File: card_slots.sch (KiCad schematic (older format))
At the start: 0 parts

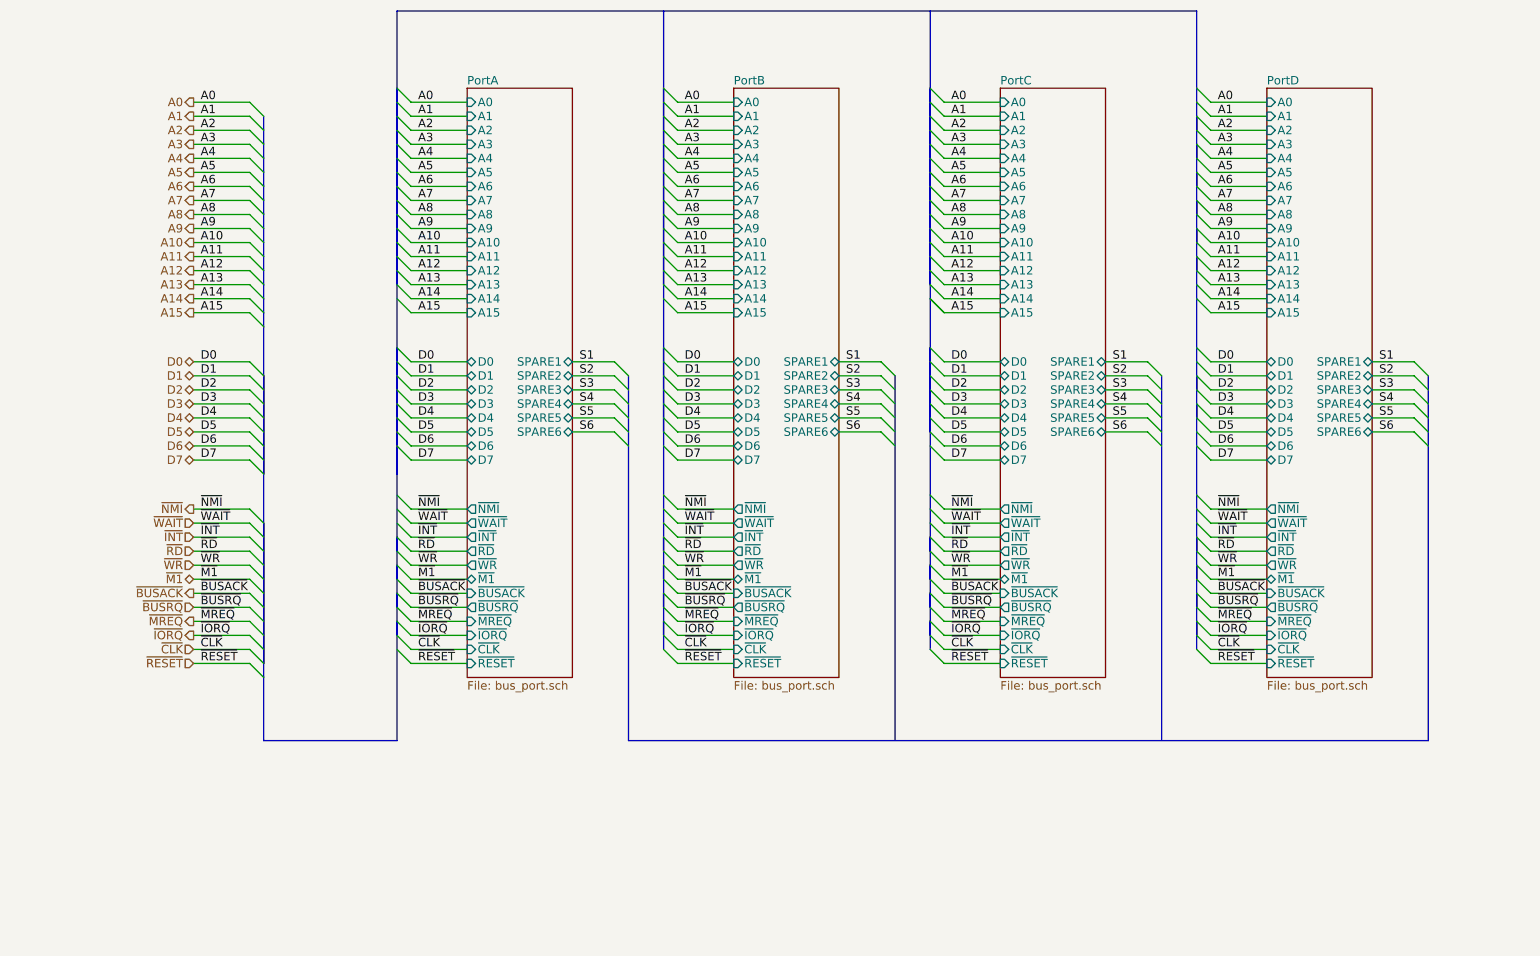
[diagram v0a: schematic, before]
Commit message: Update with smaller board and through-hole parts.
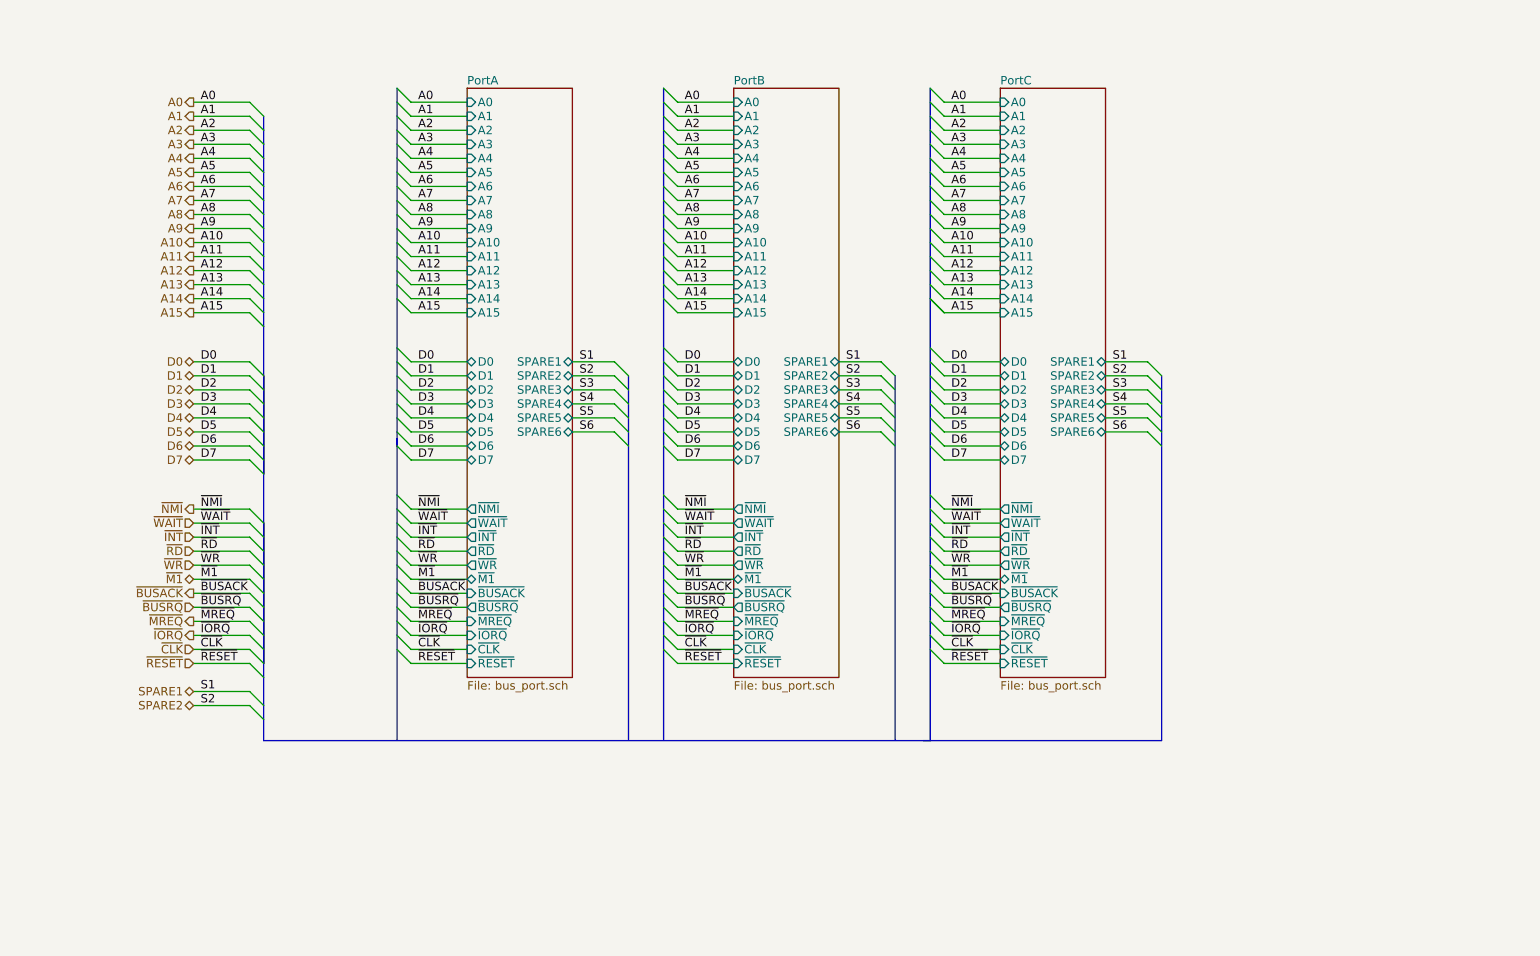
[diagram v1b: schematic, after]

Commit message: New layout complete. Now with rc2014 compat. slots!
Plus on board address decoding, single stepping using M1 line so button
is click per instruction. Board is also much smaller!
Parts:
- added C7: 100n, Capacitors_ThroughHole:C_Rect_L4_W2.5_P2.5, symbol C
- added U3: 74LS138, Housings_DIP:DIP-16_W7.62mm_LongPads, symbol 74LS138
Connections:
- net labels added: GND, RX, TX, VCC, ~IOSEL1, ~IOSEL2, ~IOSEL3, ~IOSEL4, ~IOSEL5, ~IOSEL6, ~IOSEL7, ~IOSEL8
- net labels removed: S5, S6, SPARE1, SPARE2
- wire segments 164 -> 303

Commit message: * Replaced one card slot with an updated expansion connector. * Replaced '138 with GAL. * Implemented interrupt priority lines IEI/IEO. * Replaced discrete oscillator with 14/8 pin DIP oscillator block.
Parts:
- removed U3: 74LS138, Housings_DIP:DIP-16_W7.62mm_LongPads, symbol 74LS138
- added P3: Jumper, symbol CONN_01X03
- added U3: ATF16V8CV, symbol ATF16V8CV
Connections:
- net labels added: IEI, IEO, SPARE1, SPARE2, SPARE3, SPARE4, ~IOREQ, ~IOSEL0
- net labels removed: ~IOSEL4, ~IOSEL5, ~IOSEL6, ~IOSEL7, ~IOSEL8
- wire segments 303 -> 276

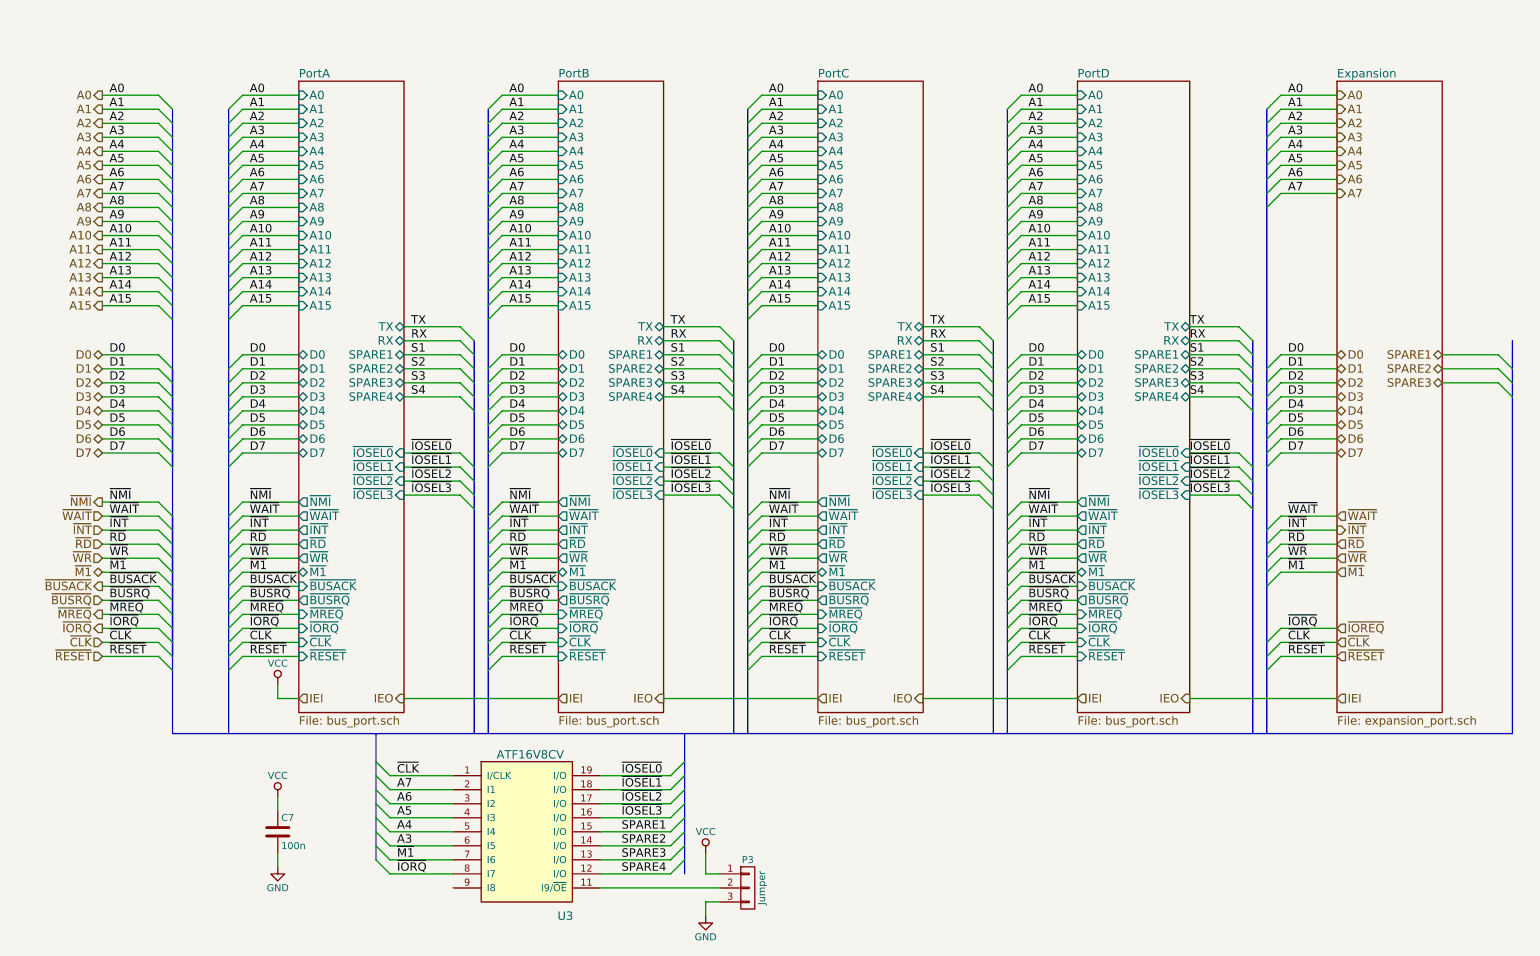
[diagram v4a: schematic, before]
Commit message: Fixed schema DRC errors
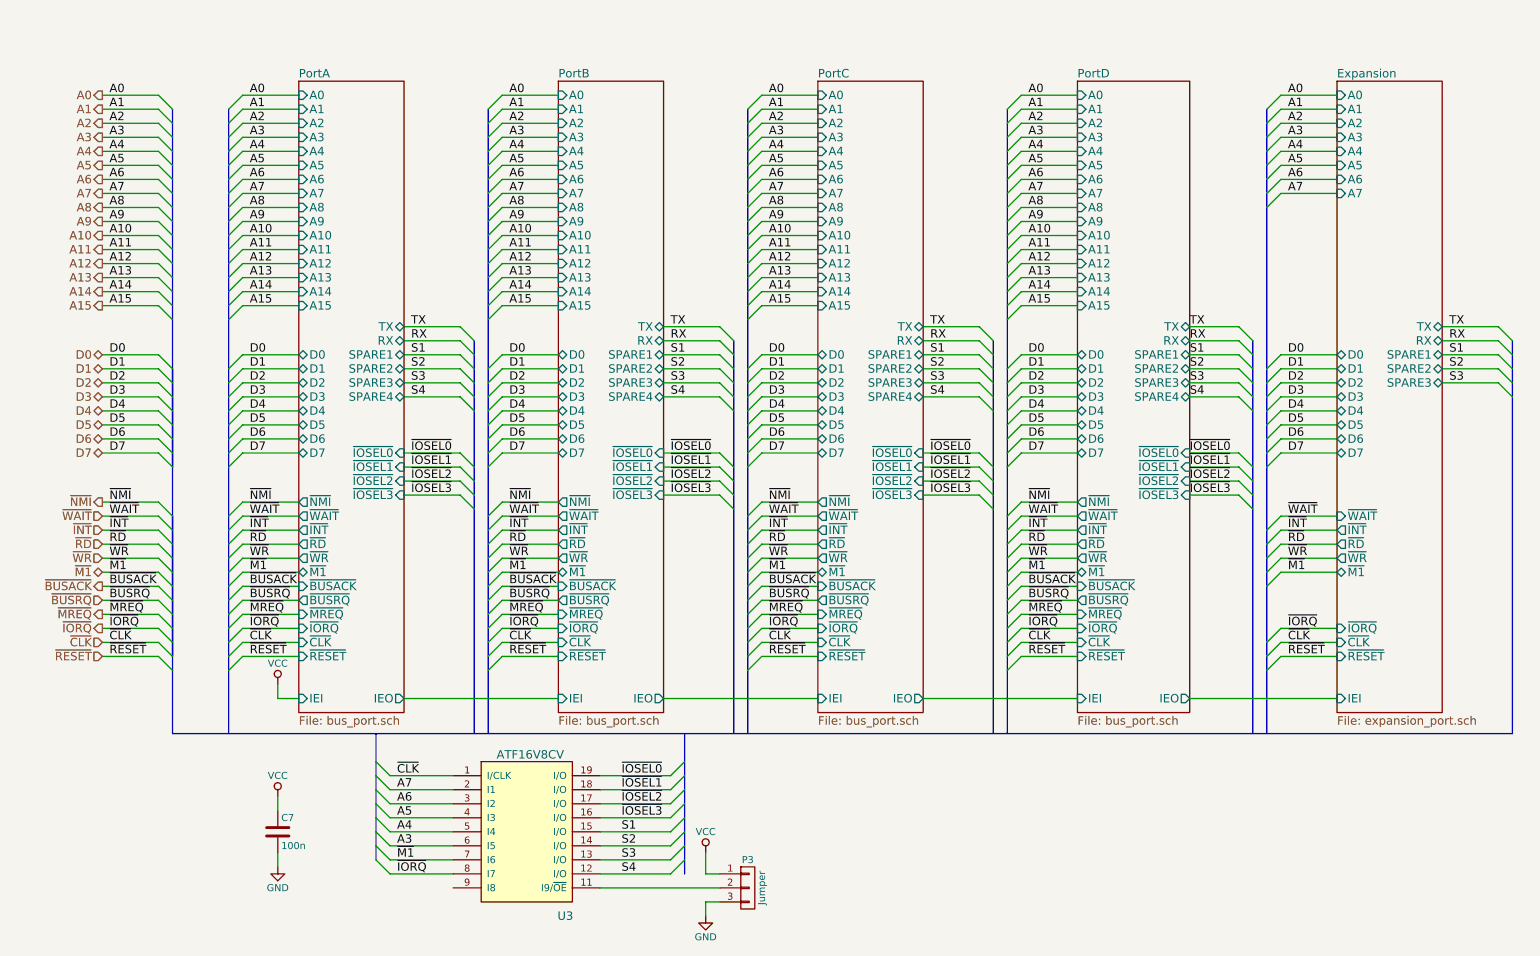
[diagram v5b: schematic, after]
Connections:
- net SPARE1 is gone; now on net S1: U3.15 (I/O)
- net SPARE2 is gone; now on net S2: U3.14 (I/O)
- net SPARE3 is gone; now on net S3: U3.13 (I/O)
- net SPARE4 is gone; now on net S4: U3.12 (I/O)
- net ~IOREQ renamed ~IORQ
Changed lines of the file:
@@
 F46 "~IOSEL2" I R 3200 4450 60
 F47 "~IOSEL3" I R 3200 4550 60
+F48 "IEI" I L 2450 6000 60
+F49 "IEO" O R 3200 6000 60
 $EndSheet
 Entry Wire Line
@@
 F46 "~IOSEL2" I R 5050 4450 60
 F47 "~IOSEL3" I R 5050 4550 60
+F48 "IEI" I L 4300 6000 60
+F49 "IEO" O R 5050 6000 60
 $EndSheet
 Entry Wire Line
@@
 F46 "~IOSEL2" I R 6900 4450 60
 F47 "~IOSEL3" I R 6900 4550 60
+F48 "IEI" I L 6150 6000 60
+F49 "IEO" O R 6900 6000 60
 $EndSheet
 Entry Wire Line
@@
 F46 "~IOSEL2" I R 8800 4450 60
 F47 "~IOSEL3" I R 8800 4550 60
+F48 "IEI" I L 8000 6000 60
+F49 "IEO" O R 8800 6000 60
 $EndSheet
 Entry Wire Line
@@
 $EndComp
 $Comp
-L VCC #PWR25
+L VCC #PWR020
 U 1 1 5797F3F2
 P 2300 6700
-F 0 "#PWR25" H 2300 6550 50  0001 C CNN
+F 0 "#PWR020" H 2300 6550 50  0001 C CNN
 F 1 "VCC" H 2300 6850 50  0000 C CNN
 F 2 "" H 2300 6700 50  0000 C CNN
@@
 $EndComp
 $Comp
-L GND #PWR26
+L GND #PWR021
 U 1 1 5797F8BA
 P 2300 7200
-F 0 "#PWR26" H 2300 6950 50  0001 C CNN
+F 0 "#PWR021" H 2300 6950 50  0001 C CNN
 F 1 "GND" H 2300 7050 50  0000 C CNN
 F 2 "" H 2300 7200 50  0000 C CNN
@@
 	1    0    0    -1
 $EndComp
-Text HLabel 2450 6000 2    60   Input ~ 0
-IEI
-Text HLabel 4300 6000 2    60   Input ~ 0
-IEI
-Text HLabel 6150 6000 2    60   Input ~ 0
-IEI
-Text HLabel 8000 6000 2    60   Input ~ 0
-IEI
-Text HLabel 3200 6000 0    60   Output ~ 0
-IEO
-Text HLabel 5050 6000 0    60   Output ~ 0
-IEO
-Text HLabel 6900 6000 0    60   Output ~ 0
-IEO
-Text HLabel 8800 6000 0    60   Output ~ 0
-IEO
 $Comp
-L VCC #PWR24
+L VCC #PWR022
 U 1 1 57AEADAF
 P 2300 5900
-F 0 "#PWR24" H 2300 5750 50  0001 C CNN
+F 0 "#PWR022" H 2300 5750 50  0001 C CNN
 F 1 "VCC" H 2300 6050 50  0000 C CNN
 F 2 "" H 2300 5900 50  0000 C CNN
@@
 	5100 7250 5200 7150
 Text Label 4750 6950 0    60   ~ 0
-SPARE1
+S1
 Text Label 4750 7050 0    60   ~ 0
-SPARE2
+S2
 Text Label 4750 7150 0    60   ~ 0
-SPARE3
+S3
 Text Label 4750 7250 0    60   ~ 0
-SPARE4
+S4
 $Comp
-L GND #PWR28
+L GND #PWR023
 U 1 1 57B78722
 P 5350 7550
-F 0 "#PWR28" H 5350 7300 50  0001 C CNN
+F 0 "#PWR023" H 5350 7300 50  0001 C CNN
 F 1 "GND" H 5350 7400 50  0000 C CNN
 F 2 "" H 5350 7550 50  0000 C CNN
@@
 $EndComp
 $Comp
-L VCC #PWR27
+L VCC #PWR024
 U 1 1 57B83991
 P 5350 7100
-F 0 "#PWR27" H 5350 6950 50  0001 C CNN
+F 0 "#PWR024" H 5350 6950 50  0001 C CNN
 F 1 "VCC" H 5350 7250 50  0000 C CNN
 F 2 "" H 5350 7100 50  0000 C CNN
@@
 	1    0    0    -1
 $EndComp
-$Sheet
-S 9850 1600 750  4500
-U 57BB639D
-F0 "Expansion" 60
-F1 "expansion_port.sch" 60
-$EndSheet
-Text HLabel 9850 1700 2    60   Output ~ 0
-A0
-Text HLabel 9850 1800 2    60   Output ~ 0
-A1
-Text HLabel 9850 1900 2    60   Output ~ 0
-A2
-Text HLabel 9850 2000 2    60   Output ~ 0
-A3
-Text HLabel 9850 2100 2    60   Output ~ 0
-A4
-Text HLabel 9850 2200 2    60   Output ~ 0
-A5
-Text HLabel 9850 2300 2    60   Output ~ 0
-A6
-Text HLabel 9850 2400 2    60   Output ~ 0
-A7
-Text HLabel 9850 3550 2    60   BiDi ~ 0
-D0
-Text HLabel 9850 3650 2    60   BiDi ~ 0
-D1
-Text HLabel 9850 3750 2    60   BiDi ~ 0
-D2
-Text HLabel 9850 3850 2    60   BiDi ~ 0
-D3
-Text HLabel 9850 3950 2    60   BiDi ~ 0
-D4
-Text HLabel 9850 4050 2    60   BiDi ~ 0
-D5
-Text HLabel 9850 4150 2    60   BiDi ~ 0
-D6
-Text HLabel 9850 4250 2    60   BiDi ~ 0
-D7
-Text HLabel 9850 4700 2    60   Input ~ 0
-~WAIT
-Text HLabel 9850 4800 2    60   Output ~ 0
-~INT
-Text HLabel 9850 4900 2    60   Input ~ 0
-~RD
-Text HLabel 9850 5000 2    60   Input ~ 0
-~WR
-Text HLabel 9850 5100 2    60   Input ~ 0
-~M1
-Text HLabel 9850 5500 2    60   Input ~ 0
-~IOREQ
-Text HLabel 9850 5600 2    60   Input ~ 0
-~CLK
-Text HLabel 9850 5700 2    60   Input ~ 0
-~RESET
 Entry Wire Line
 	11000 3550 11100 3650
@@
 Wire Wire Line
 	10600 3650 11000 3650
-Text HLabel 10600 3650 0    60   BiDi ~ 0
-SPARE2
-Text HLabel 10600 3750 0    60   BiDi ~ 0
-SPARE3
-Text HLabel 10600 3550 0    60   BiDi ~ 0
-SPARE1
 Wire Wire Line
 	10600 3550 11000 3550
-Text HLabel 9850 6000 2    60   Input ~ 0
-IEI
 Wire Wire Line
 	8800 6000 9850 6000
+$Sheet
+S 9850 1600 750  4500
+U 57BB639D
+F0 "Expansion" 60
+F1 "expansion_port.sch" 60
+F2 "A0" I L 9850 1700 60
+F3 "A1" I L 9850 1800 60
+F4 "A2" I L 9850 1900 60
+F5 "A3" I L 9850 2000 60
+F6 "A4" I L 9850 2100 60
+F7 "A5" I L 9850 2200 60
+F8 "A6" I L 9850 2300 60
+F9 "A7" I L 9850 2400 60
+F10 "D0" T L 9850 3550 60
+F11 "D1" T L 9850 3650 60
+F12 "D2" T L 9850 3750 60
+F13 "D3" T L 9850 3850 60
+F14 "D4" T L 9850 3950 60
+F15 "D5" T L 9850 4050 60
+F16 "D6" T L 9850 4150 60
+F17 "D7" T L 9850 4250 60
+F18 "~M1" T L 9850 5100 60
+F19 "~IORQ" I L 9850 5500 60
+F20 "SPARE1" B R 10600 3550 60
+F21 "SPARE2" B R 10600 3650 60
+F22 "SPARE3" B R 10600 3750 60
+F23 "~RESET" I L 9850 5700 60
+F24 "~CLK" I L 9850 5600 60
+F25 "~INT" O L 9850 4800 60
+F26 "~WR" O L 9850 5000 60
+F27 "~RD" O L 9850 4900 60
+F28 "IEI" I L 9850 6000 60
+F29 "RX" B R 10600 3450 60
+F30 "TX" B R 10600 3350 60
+F31 "~WAIT" I L 9850 4700 60
+$EndSheet
+Entry Wire Line
+	11000 3350 11100 3450
+Entry Wire Line
+	11000 3450 11100 3550
+Wire Wire Line
+	10600 3350 11000 3350
+Wire Wire Line
+	10600 3450 11000 3450
+Text Label 10650 3550 0    60   ~ 0
+S1
+Text Label 10650 3650 0    60   ~ 0
+S2
+Text Label 10650 3750 0    60   ~ 0
+S3
+Text Label 10650 3350 0    60   ~ 0
+TX
+Text Label 10650 3450 0    60   ~ 0
+RX
 $EndSCHEMATC

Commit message: Added new expansion and GAL to layout.
Haven't routed the osc. or the reset.
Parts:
- P3: footprint (none) -> Pin_Headers:Pin_Header_Straight_1x03
- U3: footprint (none) -> Housings_DIP:DIP-20_W7.62mm_LongPads
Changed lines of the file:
@@
 F 0 "U3" H 4350 5350 60  0000 C CNN
 F 1 "ATF16V8CV" H 4100 6500 60  0000 C CNN
-F 2 "" H 3750 6450 60  0000 C CNN
+F 2 "Housings_DIP:DIP-20_W7.62mm_LongPads" H 3750 6450 60  0001 C CNN
 F 3 "" H 3750 6450 60  0000 C CNN
 	1    3750 6450
@@
 F 0 "P3" H 5650 7550 50  0000 C CNN
 F 1 "Jumper" V 5750 7350 50  0000 C CNN
-F 2 "" H 5650 7350 50  0000 C CNN
+F 2 "Pin_Headers:Pin_Header_Straight_1x03" H 5650 7350 50  0001 C CNN
 F 3 "" H 5650 7350 50  0000 C CNN
 	1    5650 7350

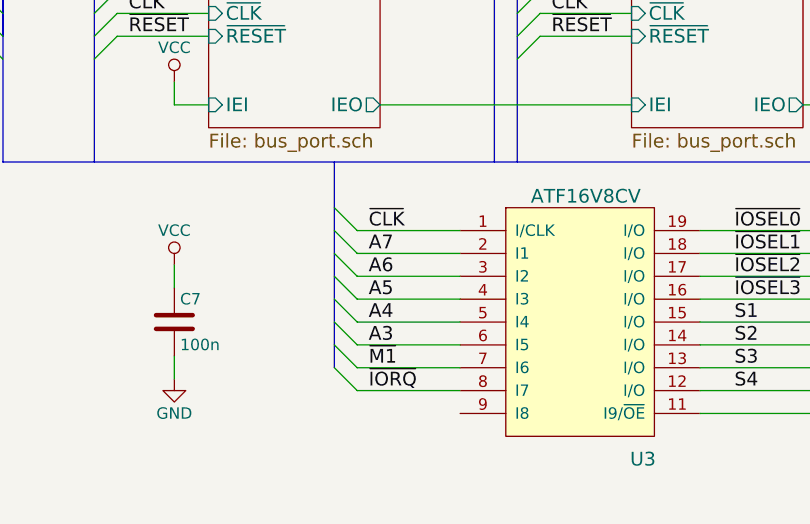
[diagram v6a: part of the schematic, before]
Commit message: Noticed missing pin I6 on GAL, added A2 input
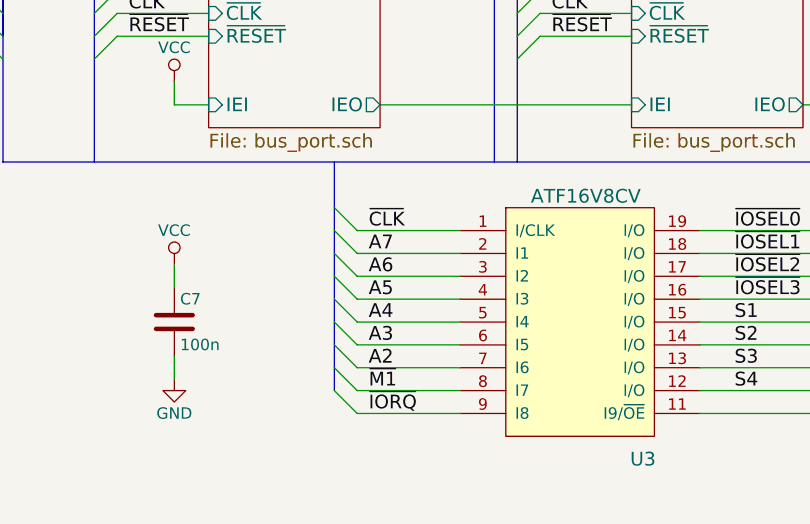
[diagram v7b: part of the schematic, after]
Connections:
- net A2: now also U3.7 (I6)
- net ~IORQ: now also U3.9 (I8); no longer U3.8 (I7)
- net ~M1: now also U3.8 (I7); no longer U3.7 (I6)
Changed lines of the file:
@@
 	3000 6750 3100 6850
 Entry Wire Line
-	3000 7050 3100 7150
-Entry Wire Line
 	3000 7150 3100 7250
-Text Label 3150 7150 0    60   ~ 0
+Entry Wire Line
+	3000 7250 3100 7350
+Text Label 3150 7250 0    60   ~ 0
 ~M1
-Text Label 3150 7250 0    60   ~ 0
+Text Label 3150 7350 0    60   ~ 0
 ~IORQ
 $Comp
@@
 	3100 6850 3550 6850
 Wire Bus Line
-	3000 6250 3000 7150
-Wire Wire Line
-	3100 7150 3550 7150
+	3000 6250 3000 7250
 Wire Wire Line
 	3100 7250 3550 7250
+Wire Wire Line
+	3100 7350 3550 7350
 Wire Bus Line
 	1550 6250 11100 6250
@@
 Text Label 10650 3450 0    60   ~ 0
 RX
+Entry Wire Line
+	3000 7050 3100 7150
+Text Label 3150 7150 0    60   ~ 0
+A2
+Wire Wire Line
+	3100 7150 3550 7150
 $EndSCHEMATC
